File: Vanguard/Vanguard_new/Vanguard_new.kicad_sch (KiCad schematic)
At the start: 72 parts, among them J1 USB_C, J2 Conn_02x03_Pin, J3 Micro_SD_Card_Det1, J4 STARBOARD_SERVO, J5 PORTSIDE_SERVO, J6 LIPO_in, Q1 BSS138, Q2 BSS138, Q3 BSS138, Q4 BSS138, U1 ATSAMD11D14A-M, U2 ATmega4809-A, U3 AT25DF641A-SH-T, U4 AP2112K-3.3, U5 MPM3610AGQV-P, U6 BNO086, U7 TXB0104D, U8 TPS61092, Y1 32.768kHz

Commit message: pcb work
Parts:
- added U9: MPM3610AGQV-P, MPM3610AGQV-P:CONV_MPM3620AGQV-P, symbol MPM3610AGQV-P:MPM3610AGQV-P
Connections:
- new net: U9.12 (PGND), U9.13 (PGND), U9.14 (PGND)
- new net: U9.19 (SW), U9.4 (SW), U9.5 (SW), U9.6 (SW)
- new net: U9.20 (OUT), U9.7 (OUT), U9.8 (OUT), U9.9 (OUT)
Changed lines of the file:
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@@
+	)
+	(symbol
+		(lib_name "MPM3610AGQV-P_1")
+		(lib_id "MPM3610AGQV-P:MPM3610AGQV-P")
+		(at 317.5 -11.43 0)
+		(unit 1)
+		(exclude_from_sim no)
+		(in_bom yes)
+		(on_board yes)
+		(dnp no)
+		(fields_autoplaced yes)
+		(property "Reference" "U9"
+			(at 317.5 -30.48 0)
+			(effects
+				(font
+					(size 1.27 1.27)
+				)
+			)
+		)
+		(property "Value" "MPM3610AGQV-P"
+			(at 317.5 -29.21 0)
+			(effects
+				(font
+					(size 1.27 1.27)
+				)
+			)
+		)
+		(property "Footprint" "MPM3610AGQV-P:CONV_MPM3620AGQV-P"
+			(at 317.5 -11.43 0)
+			(effects
+				(font
+					(size 1.27 1.27)
+				)
+				(justify bottom)
+				(hide yes)
+			)
+		)
+		(property "Datasheet" ""
+			(at 317.5 -11.43 0)
+			(effects
+				(font
+					(size 1.27 1.27)
+				)
+				(hide yes)
+			)
+		)
+		(property "Description" ""
+			(at 317.5 -11.43 0)
+			(effects
+				(font
+					(size 1.27 1.27)
+				)
+				(hide yes)
+			)
+		)
+		(property "MF" "Monolithic Power"
+			(at 317.5 -11.43 0)
+			(effects
+				(font
+					(size 1.27 1.27)
+				)
+				(justify bottom)
+				(hide yes)
+			)
+		)
+		(property "DESCRIPTION" "MPM3610A Series 21 V 1.2 A Adj. SMT Synchronous Step-Down Converter - QFN-20"
+			(at 317.5 -11.43 0)
+			(effects
+				(font
+					(size 1.27 1.27)
+				)
+				(justify bottom)
+				(hide yes)
+			)
+		)
+		(property "PACKAGE" "QFN-20 Monolithic Power Systems"
+			(at 317.5 -11.43 0)
+			(effects
+				(font
+					(size 1.27 1.27)
+				)
+				(justify bottom)
+				(hide yes)
+			)
+		)
+		(property "PRICE" "2.62 USD"
+			(at 317.5 -11.43 0)
+			(effects
+				(font
+					(size 1.27 1.27)
+				)
+				(justify bottom)
+				(hide yes)
+			)
+		)
+		(property "Package" "QFN-20 MPS"
+			(at 317.5 -11.43 0)
+			(effects
+				(font
+					(size 1.27 1.27)
+				)
+				(justify bottom)
+				(hide yes)
+			)
+		)
+		(property "Check_prices" "https://www.snapeda.com/parts/MPM3610AGQV-P/Monolithic+Power+Systems+Inc./view-part/?ref=eda"
+			(at 317.5 -11.43 0)
+			(effects
+				(font
+					(size 1.27 1.27)
+				)
+				(justify bottom)
+				(hide yes)
+			)
+		)
+		(property "STANDARD" "Manufacturer recommendation"
+			(at 317.5 -11.43 0)
+			(effects
+				(font
+					(size 1.27 1.27)
+				)
+				(justify bottom)
+				(hide yes)
+			)
+		)
+		(property "PARTREV" "1.0"
+			(at 317.5 -11.43 0)
+			(effects
+				(font
+					(size 1.27 1.27)
+				)
+				(justify bottom)
+				(hide yes)
+			)
+		)
+		(property "SnapEDA_Link" "https://www.snapeda.com/parts/MPM3610AGQV-P/Monolithic+Power+Systems+Inc./view-part/?ref=snap"
+			(at 317.5 -11.43 0)
+			(effects
+				(font
+					(size 1.27 1.27)
+				)
+				(justify bottom)
+				(hide yes)
+			)
+		)
+		(property "MP" "MPM3610AGQV-P"
+			(at 317.5 -11.43 0)
+			(effects
+				(font
+					(size 1.27 1.27)
+				)
+				(justify bottom)
+				(hide yes)
+			)
+		)
+		(property "Price" "None"
+			(at 317.5 -11.43 0)
+			(effects
+				(font
+					(size 1.27 1.27)
+				)
+				(justify bottom)
+				(hide yes)
+			)
+		)
+		(property "Availability" "In Stock"
+			(at 317.5 -11.43 0)
+			(effects
+				(font
+					(size 1.27 1.27)
+				)
+				(justify bottom)
+				(hide yes)
+			)
+		)
+		(property "AVAILABILITY" "Bad"
+			(at 317.5 -11.43 0)
+			(effects
+				(font
+					(size 1.27 1.27)
+				)
+				(justify bottom)
+				(hide yes)
+			)
+		)
+		(property "Description_1" "\nNon-Isolated PoL Module DC DC Converter 1 Output 0.8 ~ 18.48V - - - 1.2A 4.5V - 21V Input\n"
+			(at 317.5 -11.43 0)
+			(effects
+				(font
+					(size 1.27 1.27)
+				)
+				(justify bottom)
+				(hide yes)
+			)
+		)
+		(pin "4"
+		)
+		(pin "9"
+		)
+		(pin "8"
+		)
+		(pin "2"
+		)
+		(pin "5"
+		)
+		(pin "6"
+		)
+		(pin "3"
+		)
+		(pin "1"
+		)
+		(pin "13"
+		)
+		(pin "12"
+		)
+		(pin "14"
+		)
+		(pin "11"
+		)
+		(pin "7"
+		)
+		(pin "19"
+		)
+		(pin "16"
+		)
+		(pin "20"
+		)
+		(pin "18"
+		)
+		(pin "17"
+		)
+		(instances
+			(project ""
+				(path "/972fbf12-2dcd-4fdf-b1c9-8a2880c46640"
+					(reference "U9")
+					(unit 1)
+				)
+			)
+		)
 	)
 	(symbol

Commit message: just in case push
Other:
- moved on the sheet: U9
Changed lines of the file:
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@@
 		(lib_name "MPM3610AGQV-P_1")
 		(lib_id "MPM3610AGQV-P:MPM3610AGQV-P")
-		(at 317.5 -11.43 0)
+		(at 306.07 10.16 0)
 		(unit 1)
 		(exclude_from_sim no)
@@
 		(fields_autoplaced yes)
 		(property "Reference" "U9"
-			(at 317.5 -30.48 0)
+			(at 306.07 -8.89 0)
 			(effects
 				(font
@@
 		)
 		(property "Value" "MPM3610AGQV-P"
-			(at 317.5 -29.21 0)
+			(at 306.07 -7.62 0)
 			(effects
 				(font
@@
 		)
 		(property "Footprint" "MPM3610AGQV-P:CONV_MPM3620AGQV-P"
-			(at 317.5 -11.43 0)
+			(at 306.07 10.16 0)
 			(effects
 				(font
@@
 		)
 		(property "Datasheet" ""
-			(at 317.5 -11.43 0)
+			(at 306.07 10.16 0)
 			(effects
 				(font
@@
 		)
 		(property "Description" ""
-			(at 317.5 -11.43 0)
+			(at 306.07 10.16 0)
 			(effects
 				(font
@@
 		)
 		(property "MF" "Monolithic Power"
-			(at 317.5 -11.43 0)
+			(at 306.07 10.16 0)
 			(effects
 				(font
@@
 		)
 		(property "DESCRIPTION" "MPM3610A Series 21 V 1.2 A Adj. SMT Synchronous Step-Down Converter - QFN-20"
-			(at 317.5 -11.43 0)
+			(at 306.07 10.16 0)
 			(effects
 				(font
@@
 		)
 		(property "PACKAGE" "QFN-20 Monolithic Power Systems"
-			(at 317.5 -11.43 0)
+			(at 306.07 10.16 0)
 			(effects
 				(font
@@
 		)
 		(property "PRICE" "2.62 USD"
-			(at 317.5 -11.43 0)
+			(at 306.07 10.16 0)
 			(effects
 				(font
@@
 		)
 		(property "Package" "QFN-20 MPS"
-			(at 317.5 -11.43 0)
+			(at 306.07 10.16 0)
 			(effects
 				(font
@@
 		)
 		(property "Check_prices" "https://www.snapeda.com/parts/MPM3610AGQV-P/Monolithic+Power+Systems+Inc./view-part/?ref=eda"
-			(at 317.5 -11.43 0)
+			(at 306.07 10.16 0)
 			(effects
 				(font
@@
 		)
 		(property "STANDARD" "Manufacturer recommendation"
-			(at 317.5 -11.43 0)
+			(at 306.07 10.16 0)
 			(effects
 				(font
@@
 		)
 		(property "PARTREV" "1.0"
-			(at 317.5 -11.43 0)
+			(at 306.07 10.16 0)
 			(effects
 				(font
@@
 		)
 		(property "SnapEDA_Link" "https://www.snapeda.com/parts/MPM3610AGQV-P/Monolithic+Power+Systems+Inc./view-part/?ref=snap"
-			(at 317.5 -11.43 0)
+			(at 306.07 10.16 0)
 			(effects
 				(font
@@
 		)
 		(property "MP" "MPM3610AGQV-P"
-			(at 317.5 -11.43 0)
+			(at 306.07 10.16 0)
 			(effects
 				(font
@@
 		)
 		(property "Price" "None"
-			(at 317.5 -11.43 0)
+			(at 306.07 10.16 0)
 			(effects
 				(font
@@
 		)
 		(property "Availability" "In Stock"
-			(at 317.5 -11.43 0)
+			(at 306.07 10.16 0)
 			(effects
 				(font
@@
 		)
 		(property "AVAILABILITY" "Bad"
-			(at 317.5 -11.43 0)
+			(at 306.07 10.16 0)
 			(effects
 				(font
@@
 		)
 		(property "Description_1" "\nNon-Isolated PoL Module DC DC Converter 1 Output 0.8 ~ 18.48V - - - 1.2A 4.5V - 21V Input\n"
-			(at 317.5 -11.43 0)
+			(at 306.07 10.16 0)
 			(effects
 				(font

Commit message: usb input almost done
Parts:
- removed U9: MPM3610AGQV-P, MPM3610AGQV-P:CONV_MPM3620AGQV-P, symbol MPM3610AGQV-P:MPM3610AGQV-P
- J2: footprint Connector_PinHeader_2.54mm:PinHeader_1x03_P2.54mm_Vertical -> Connector_PinHeader_2.54mm:PinHeader_2x03_P2.54mm_Vertical
- J6: footprint CONN2_2601-1102_WAG -> Wago-2601-1102:CONN2_2601-1102_WAG

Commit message: pcb laying out
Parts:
- removed J6: LIPO_in, Wago-2601-1102:CONN2_2601-1102_WAG, symbol 2024-10-24_18-37-30:2601-1102
- added J6: Conn_01x02_Pin, Connector_PinHeader_2.54mm:PinHeader_1x02_P2.54mm_Vertical, symbol Connector:Conn_01x02_Pin
- TP1, TP2: footprint TestPoint:TestPoint_2Pads_Pitch5.08mm_Drill1.3mm -> TestPoint:TestPoint_Pad_1.0x1.0mm
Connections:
- net GND: now also J6.2 (Pin_2)
- net VCC: now also J6.1 (Pin_1)
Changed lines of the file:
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@@
 	(wire
 		(pts
-			(xy 339.09 167.64) (xy 339.09 170.18)
+			(xy 339.09 166.37) (xy 339.09 170.18)
 		)
 		(stroke
@@
 	(wire
 		(pts
+			(xy 339.09 162.56) (xy 339.09 163.83)
+		)
+		(stroke
+			(width 0)
+			(type default)
+		)
+	)
+	(wire
+		(pts
 			(xy 311.15 119.38) (xy 317.5 119.38)
 		)
@@
 	)
 	(symbol
-		(lib_id "2024-10-24_18-37-30:2601-1102")
-		(at 339.09 167.64 180)
-		(unit 1)
-		(exclude_from_sim no)
-		(in_bom yes)
-		(on_board yes)
-		(dnp no)
-		(fields_autoplaced yes)
-		(property "Reference" "J6"
-			(at 330.2 152.4 0)
-			(effects
-				(font
-					(size 1.27 1.27)
-				)
-			)
-		)
-		(property "Value" "LIPO_in"
-			(at 330.2 154.94 0)
-			(effects
-				(font
-					(size 1.27 1.27)
-				)
-			)
-		)
-		(property "Footprint" "Wago-2601-1102:CONN2_2601-1102_WAG"
-			(at 339.09 167.64 0)
-			(effects
-				(font
-					(size 1.27 1.27)
-					(italic yes)
-				)
-				(hide yes)
-			)
-		)
-		(property "Datasheet" "2601-1102"
-			(at 339.09 167.64 0)
-			(effects
-				(font
-					(size 1.27 1.27)
-					(italic yes)
-				)
-				(hide yes)
-			)
-		)
-		(property "Description" "Generic screw terminal, single row, 01x02, script generated (kicad-library-utils/schlib/autogen/connector/)"
-			(at 339.09 167.64 0)
-			(effects
-				(font
-					(size 1.27 1.27)
-				)
-				(hide yes)
-			)
-		)
-		(pin "1"
-		)
-		(pin "2"
-		)
-		(pin "3"
-		)
-		(pin "4"
-		)
-		(instances
-			(project ""
-				(path "/972fbf12-2dcd-4fdf-b1c9-8a2880c46640"
-					(reference "J6")
-					(unit 1)
-				)
-			)
-		)
-	)
-	(symbol
 		(lib_id "Connector:Conn_01x03_Pin")
 		(at 284.48 163.83 270)
@@
 			)
 		)
-		(property "Footprint" "TestPoint:TestPoint_2Pads_Pitch5.08mm_Drill1.3mm"
+		(property "Footprint" "TestPoint:TestPoint_Pad_1.0x1.0mm"
 			(at 59.69 41.91 0)
 			(effects
@@
 	)
 	(symbol
+		(lib_id "Connector:Conn_01x02_Pin")
+		(at 334.01 163.83 0)
+		(unit 1)
+		(exclude_from_sim no)
+		(in_bom yes)
+		(on_board yes)
+		(dnp no)
+		(fields_autoplaced yes)
+		(property "Reference" "J6"
+			(at 334.645 158.75 0)
+			(effects
+				(font
+					(size 1.27 1.27)
+				)
+			)
+		)
+		(property "Value" "Conn_01x02_Pin"
+			(at 334.645 161.29 0)
+			(effects
+				(font
+					(size 1.27 1.27)
+				)
+			)
+		)
+		(property "Footprint" "Connector_PinHeader_2.54mm:PinHeader_1x02_P2.54mm_Vertical"
+			(at 334.01 163.83 0)
+			(effects
+				(font
+					(size 1.27 1.27)
+				)
+				(hide yes)
+			)
+		)
+		(property "Datasheet" "~"
+			(at 334.01 163.83 0)
+			(effects
+				(font
+					(size 1.27 1.27)
+				)
+				(hide yes)
+			)
+		)
+		(property "Description" "Generic connector, single row, 01x02, script generated"
+			(at 334.01 163.83 0)
+			(effects
+				(font
+					(size 1.27 1.27)
+				)
+				(hide yes)
+			)
+		)
+		(pin "2"
+		)
+		(pin "1"
+		)
+		(instances
+			(project ""
+				(path "/972fbf12-2dcd-4fdf-b1c9-8a2880c46640"
+					(reference "J6")
+					(unit 1)
+				)
+			)
+		)
+	)
+	(symbol
 		(lib_id "Device:R")
 		(at 58.42 156.21 90)
@@
 			)
 		)
-		(property "Footprint" "TestPoint:TestPoint_2Pads_Pitch5.08mm_Drill1.3mm"
+		(property "Footprint" "TestPoint:TestPoint_Pad_1.0x1.0mm"
 			(at 97.79 26.67 0)
 			(effects

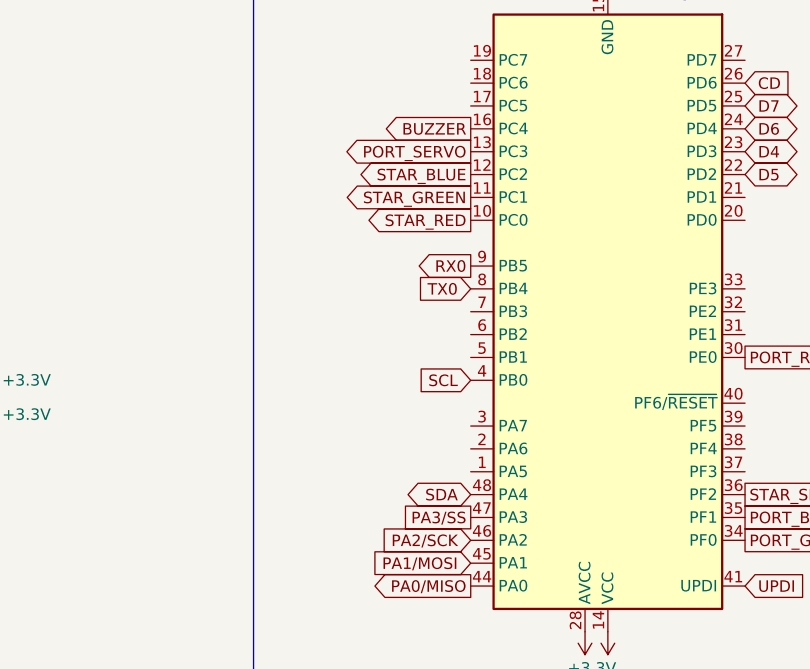
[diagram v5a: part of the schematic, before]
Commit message: fixed sca pin and cleared some track-via clearnace issues
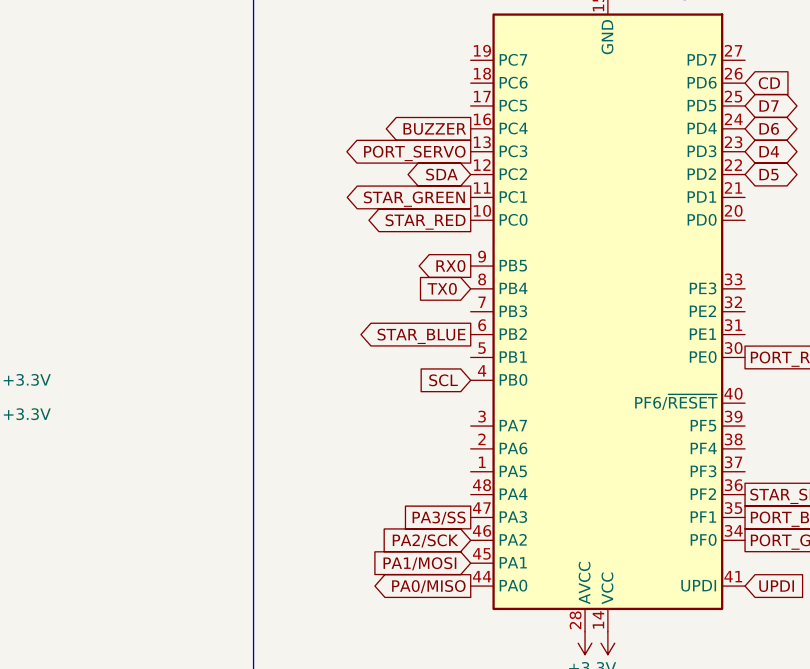
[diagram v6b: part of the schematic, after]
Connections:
- net SDA: now also U2.12 (PC2); no longer U2.48 (PA4)
- net STAR_BLUE: now also U2.6 (PB2); no longer U2.12 (PC2)
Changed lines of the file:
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@@
-		)
-	)
-	(global_label "SDA"
-		(shape bidirectional)
-		(at 213.36 167.64 180)
-		(fields_autoplaced yes)
-		(effects
-			(font
-				(size 1.27 1.27)
-			)
-			(justify right)
-		)
-		(property "Intersheetrefs" "${INTERSHEET_REFS}"
-			(at 205.6954 167.64 0)
-			(effects
-				(font
-					(size 1.27 1.27)
-				)
-				(justify right)
-				(hide yes)
-			)
 		)
 	)
@@
 		)
 	)
+	(global_label "SDA"
+		(shape bidirectional)
+		(at 213.36 132.08 180)
+		(fields_autoplaced yes)
+		(effects
+			(font
+				(size 1.27 1.27)
+			)
+			(justify right)
+		)
+		(property "Intersheetrefs" "${INTERSHEET_REFS}"
+			(at 205.6954 132.08 0)
+			(effects
+				(font
+					(size 1.27 1.27)
+				)
+				(justify right)
+				(hide yes)
+			)
+		)
+	)
 	(global_label "PA3{slash}SS"
 		(shape passive)
@@
 	(global_label "STAR_BLUE"
 		(shape output)
-		(at 213.36 132.08 180)
-		(fields_autoplaced yes)
-		(effects
-			(font
-				(size 1.27 1.27)
-			)
-			(justify right)
-		)
-		(property "Intersheetrefs" "${INTERSHEET_REFS}"
-			(at 200.0939 132.08 0)
-			(effects
-				(font
+		(at 213.36 149.86 180)
+		(fields_autoplaced yes)
+		(effects
+			(font
+				(size 1.27 1.27)
+			)
+			(justify right)
+		)
+		(property "Intersheetrefs" "${INTERSHEET_REFS}"
+			(at 200.0939 149.86 0)
+			(effects
+				(font

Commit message: fixed many errors
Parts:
- removed J4: STARBOARD_SERVO, Connector_PinHeader_2.54mm:PinHeader_1x03_P2.54mm_Vertical, symbol Connector:Conn_01x03_Pin
- removed J5: PORTSIDE_SERVO, Connector_PinHeader_2.54mm:PinHeader_1x03_P2.54mm_Vertical, symbol Connector:Conn_01x03_Pin
- added J4: STARBOARD_SERVO, Connector_PinHeader_2.54mm:PinHeader_1x03_P2.54mm_Vertical, symbol Connector_Generic:Conn_01x03
- added J5: PORTSIDE_SERVO, Connector_PinHeader_2.54mm:PinHeader_1x03_P2.54mm_Vertical, symbol Connector_Generic:Conn_01x03
- U8: footprint Package_DFN_QFN:Texas_RSA_VQFN-16-1EP_4x4mm_P0.65mm_EP2.7x2.7mm_ThermalVias -> Package_DFN_QFN:DFN-10-1EP_3x3mm_P0.5mm_EP1.65x2.38mm_ThermalVias
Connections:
- net +5V: now also J4.2 (Pin_2), J5.2 (Pin_2)
- net GND: now also J4.3 (Pin_3), J5.3 (Pin_3)
- net PORT_SERVO: now also J5.1 (Pin_1)
- net STAR_SERVO: now also J4.1 (Pin_1)
